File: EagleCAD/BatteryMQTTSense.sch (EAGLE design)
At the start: 11 parts, among them U2 Si7021-A20

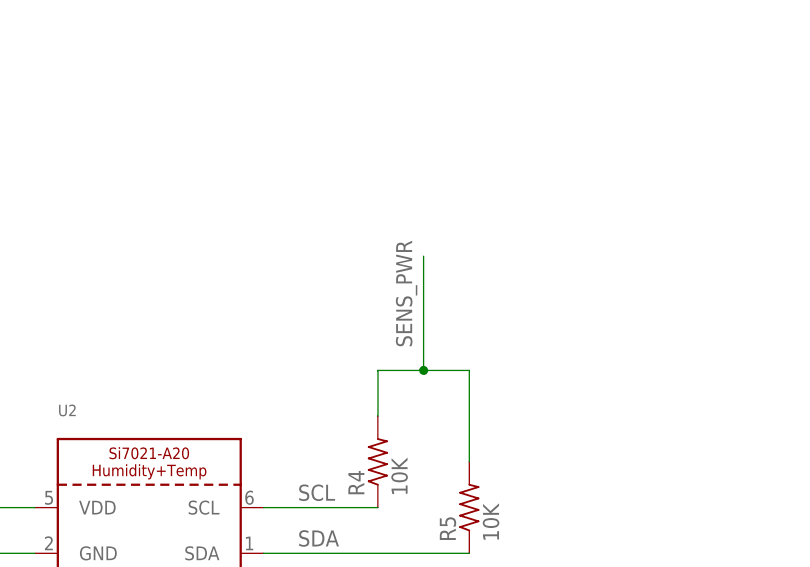
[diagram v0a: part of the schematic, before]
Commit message: pushing validated version of board and firmware, including stl files for enclosure
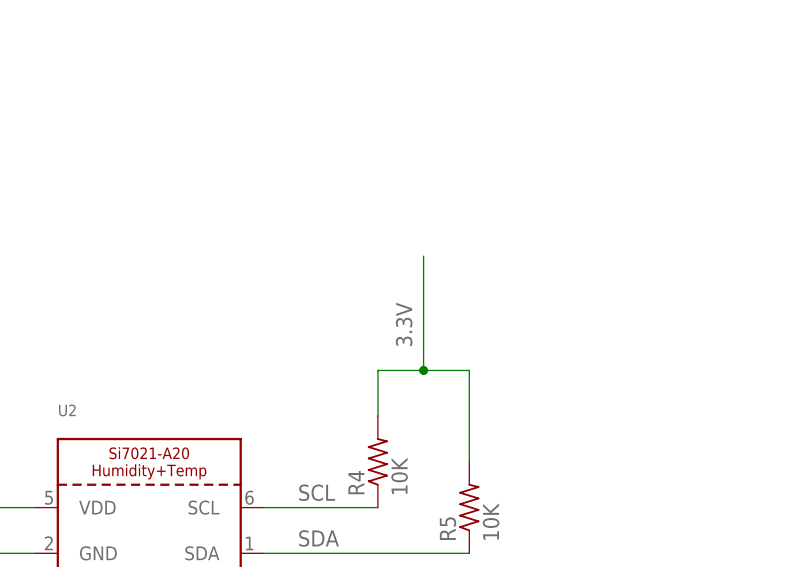
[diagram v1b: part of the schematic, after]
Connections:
- net 3.3V: now also R4.2, R5.2
- net SENS_PWR: no longer R4.2, R5.2
